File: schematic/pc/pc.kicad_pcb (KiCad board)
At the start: 2 copper layers, 24.8 x 23.5 mm, 3 parts, among them P1 USB_A, P2 USB_A, P3 USB_A

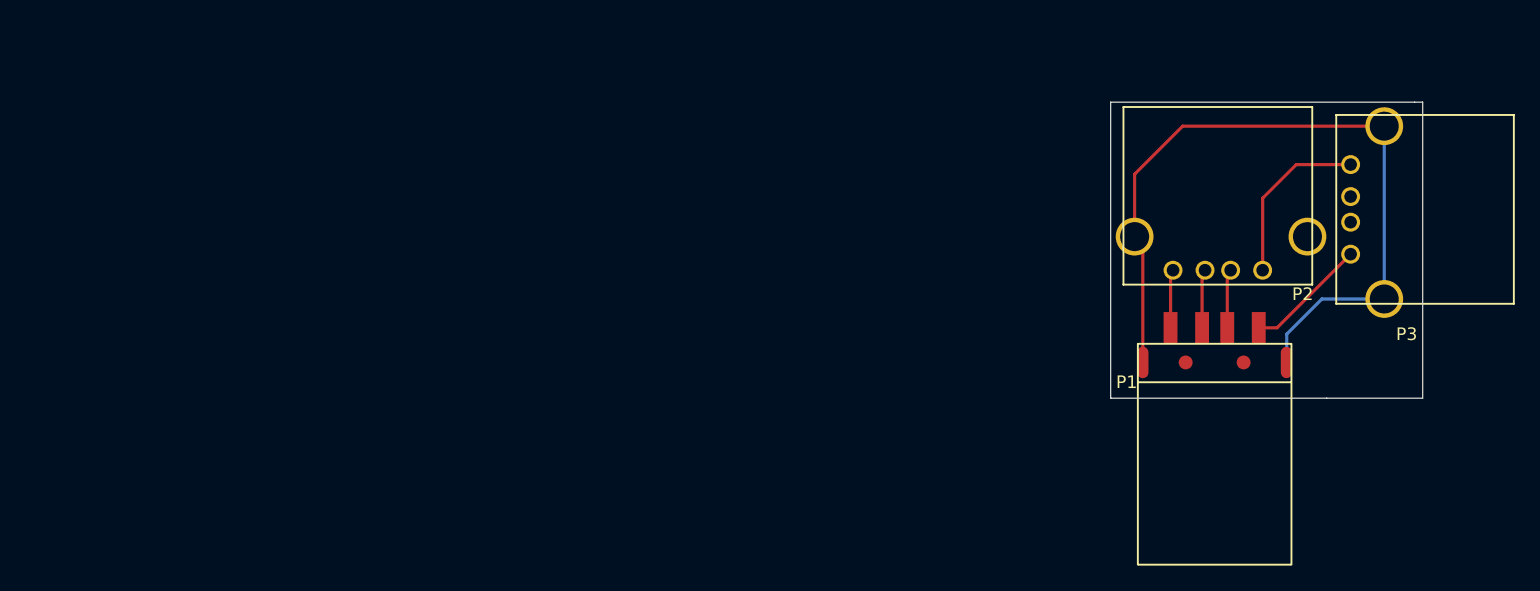
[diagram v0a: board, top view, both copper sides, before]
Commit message: Switched PC board to wired male
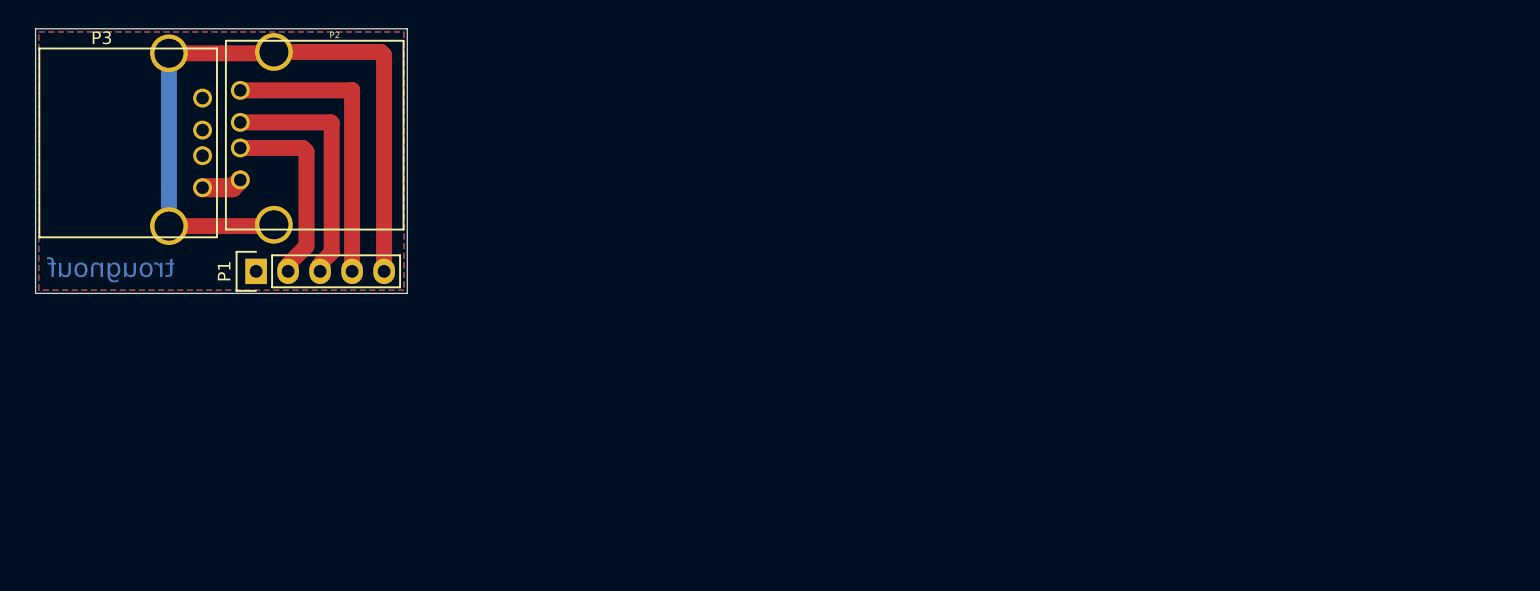
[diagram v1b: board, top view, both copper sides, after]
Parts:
- P1: footprint con-trougnouf:USB_A -> Pin_Headers:Pin_Header_Straight_1x05
- moved P3 92.0 mm to (115.2, 123.5), turned to 270 degrees
- moved P2 81.5 mm to (118.2, 130.0), turned to 90 degrees
- moved P1 76.6 mm to (119.5, 137.2), turned to 90 degrees
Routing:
- net Net-(P1-Pad4): track 4.65 -> 23.3 mm
- net Net-(P1-Pad3): track 4.67 -> 19.4 mm
- net Net-(P1-Pad2): track 4.68 -> 15.5 mm
- net Net-(P2-Pad1): track 13.8 -> 3.25 mm
- net Net-(P1-Pad1): track 9.90 -> 0.00 mm
- net Net-(P1-Pad5): track 62.1 -> 56.5 mm
- added copper zone on B.Cu, net Net-(P1-Pad1)
- added copper zone on F.Cu, net Net-(P1-Pad4)
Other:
- board size 24.8 x 23.5 mm -> 29.5 x 21 mm
- net class Default: trace_width 0.25 -> 0.3048
- net class huge added: clearance 0.2, trace_width 1.524, via_dia 0.6, via_drill 0.4
- net class large added: clearance 0.2, trace_width 1.27, via_dia 0.6, via_drill 0.4
- rule trace_min: 0.2 -> 0.3048
- board text added: "GND"
- board text added: "KB"
- board text added: "PC"
- board text added: "SW"
- board text added: "USB-SW(PC) 1.01"
- board text added: "VCC"
- board text removed: "Keyboard"
- board text removed: "Switch"
- board text removed: "USB Switch 1.00"
- board text removed: "USB-SW"
